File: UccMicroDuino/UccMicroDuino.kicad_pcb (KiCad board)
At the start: 2 copper layers, 8 parts, among them J1 Conn_01x10_Socket, J2 USB_A, U1 ATtiny85-20S

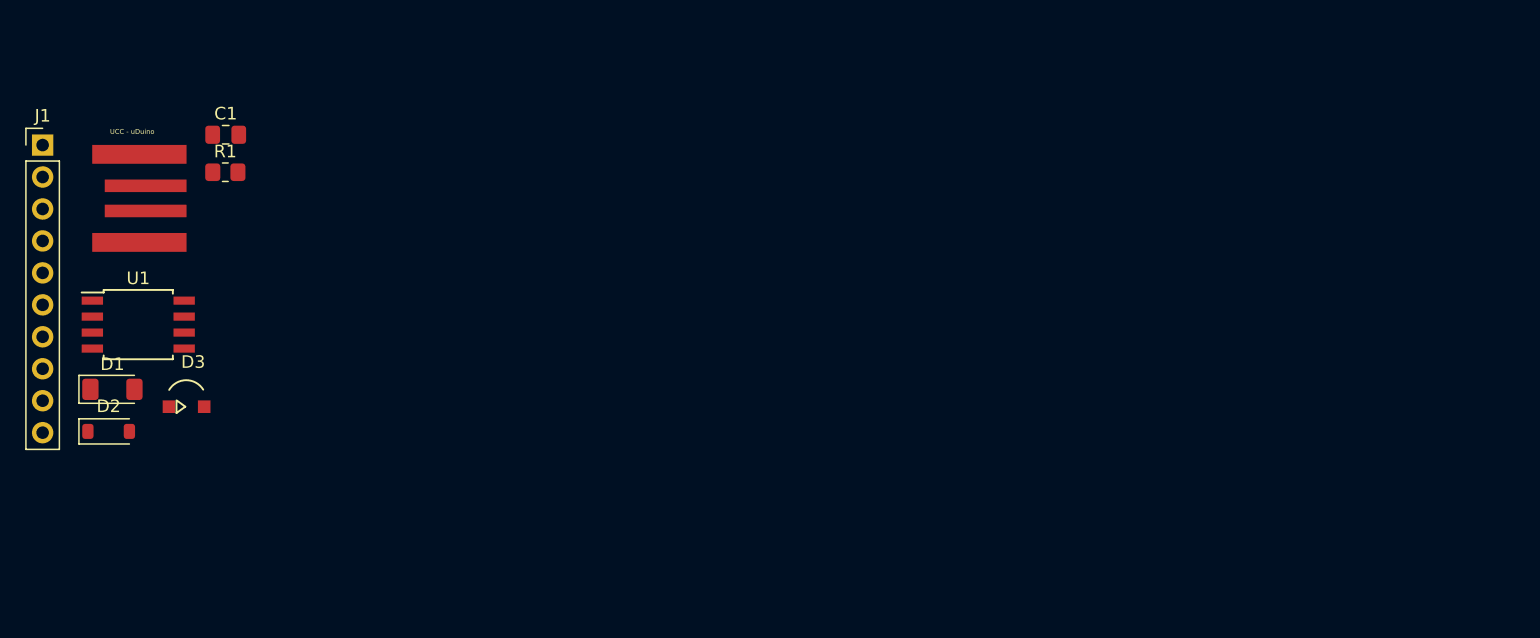
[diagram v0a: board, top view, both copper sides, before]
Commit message: Add files via upload
Subimos el archivo kicad.
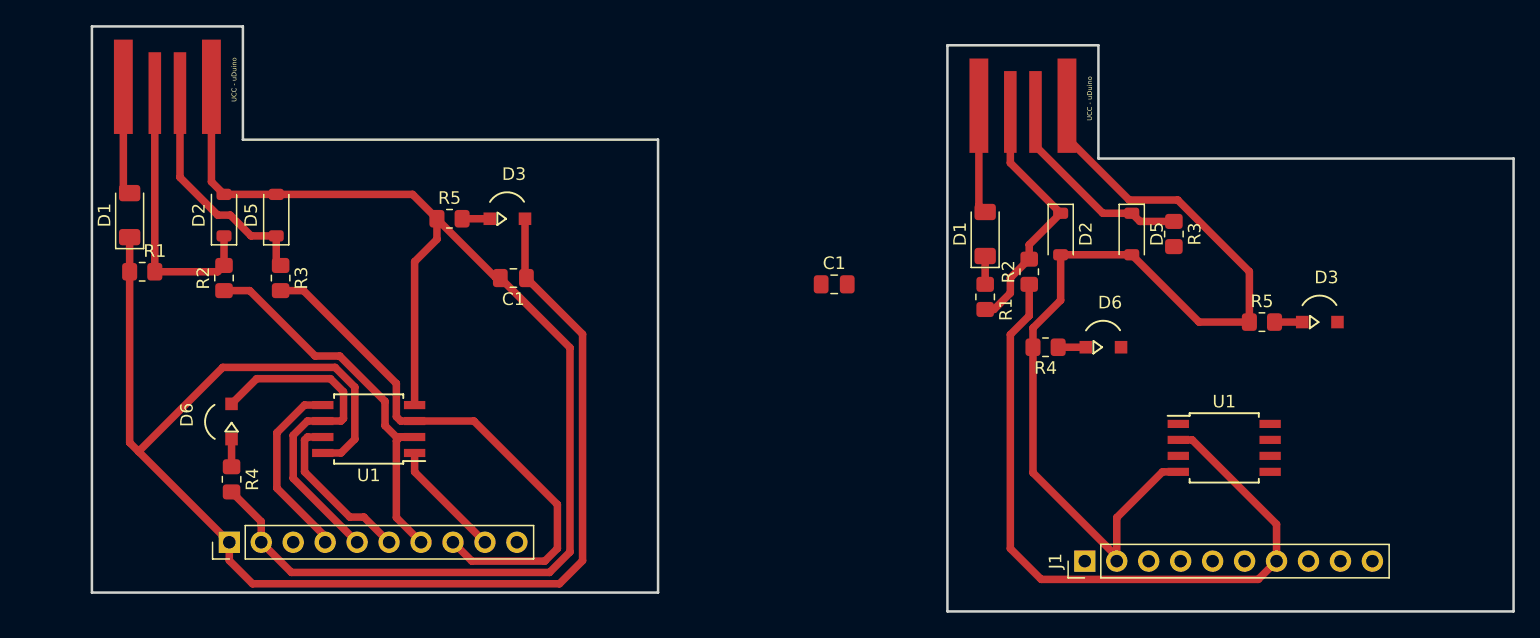
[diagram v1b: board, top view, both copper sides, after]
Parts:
- added C1: C, Capacitor_SMD:C_0805_2012Metric_Pad1.18x1.45mm_HandSolder, F.Cu at (161.5, 78.5)
- added D1: PMLL4148L, Diode_SMD:D_MiniMELF, F.Cu at (131.0, 73.5)
- added D2: 3.6V 1/2mW, Diode_SMD:D_SOD-123, F.Cu at (138.5, 73.5)
- added D3: LED, ledSmd:ledSMD, F.Cu at (161.4, 73.8)
- added D5: 3.6V 1/2mW, Diode_SMD:D_SOD-123, F.Cu at (210.7, 75.0)
- added D5: 3.6V 1/2mW, Diode_SMD:D_SOD-123, F.Cu at (142.7, 73.5)
- added D6: Led Greeen, ledSmd:ledSMD, F.Cu at (139.1, 89.5)
- added D6: Led Greeen, ledSmd:ledSMD, F.Cu at (208.8, 84.0)
- added J1: Header, Connector_PinHeader_2.54mm:PinHeader_1x10_P2.54mm_Vertical, F.Cu at (138.9, 99.5)
- added J2: USB_A, embeddedPcbUsb:USB_A_UCC, F.Cu at (134.0, 63.5)
- added R1: 1.5KΩ 5% 1/8W, Resistor_SMD:R_0805_2012Metric_Pad1.20x1.40mm_HandSolder, F.Cu at (132.0, 78.0)
- added R2: 68 Ω 5% 1/8W, Resistor_SMD:R_0805_2012Metric_Pad1.20x1.40mm_HandSolder, F.Cu at (202.5, 78.0)
- added R2: 68 Ω 5% 1/8W, Resistor_SMD:R_0805_2012Metric_Pad1.20x1.40mm_HandSolder, F.Cu at (138.5, 78.5)
- added R3: 68 Ω 5% 1/8W, Resistor_SMD:R_0805_2012Metric_Pad1.20x1.40mm_HandSolder, F.Cu at (143.0, 78.5)
- added R3: 68 Ω 5% 1/8W, Resistor_SMD:R_0805_2012Metric_Pad1.20x1.40mm_HandSolder, F.Cu at (214.0, 75.0)
- added R4: 330Ω 5%1/8W, Resistor_SMD:R_0805_2012Metric_Pad1.20x1.40mm_HandSolder, F.Cu at (203.8, 84.0)
- added R4: 330Ω 5%1/8W, Resistor_SMD:R_0805_2012Metric_Pad1.20x1.40mm_HandSolder, F.Cu at (139.1, 94.5)
- added R5: 330Ω 5%1/8W, Resistor_SMD:R_0805_2012Metric_Pad1.20x1.40mm_HandSolder, F.Cu at (221.0, 82.0)
- added R5: 330Ω 5%1/8W, Resistor_SMD:R_0805_2012Metric_Pad1.20x1.40mm_HandSolder, F.Cu at (156.4, 73.8)
- added U1: ATtiny85-20S, Package_SO:SOIC-8W_5.3x5.3mm_P1.27mm, F.Cu at (150.0, 90.5)
- D1: value D_Filled -> PMLL4148L
- D2: value D_Zener -> 3.6V 1/2mW
- J1: value Conn_01x10_Socket -> Header
- R1: value R -> 1.5KΩ 5% 1/8W
- moved D3 90.3 mm to (226.0, 82.0)
- moved J1 89.2 mm to (206.9, 101.0), turned to 90 degrees
- moved U1 86.9 mm to (218.0, 92.0)
- moved D2 77.3 mm to (205.0, 75.0), turned to -90 degrees
- moved D1 70.5 mm to (199.0, 75.0), turned to 90 degrees
- moved J2 70.4 mm to (202.0, 65.0), turned to -90 degrees
- moved R1 61.2 mm to (199.0, 80.0), turned to -90 degrees
- moved C1 49.8 mm to (187.0, 79.0)
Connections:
- C1 pad 1: unconnected-(C1-Pad1) -> +5V
- C1 pad 2: unconnected-(C1-Pad2) -> GND
- D1 pad 2: unconnected-(D1-A-Pad2) -> Net-(D1-A)
- D2 pad 1: unconnected-(D2-K-Pad1) -> Net-(D2-K)
- D2 pad 2: unconnected-(D2-A-Pad2) -> GND
- D3 pad 1: unconnected-(D3-K-Pad1) -> Net-(D3-K)
- D3 pad 2: unconnected-(D3-A-Pad2) -> +5V
- J1 pad 1: unconnected-(J1-Pin_1-Pad1) -> +5V
- J1 pad 2: unconnected-(J1-Pin_2-Pad2) -> GND
- J1 pad 4: unconnected-(J1-Pin_4-Pad4) -> Net-(J1-Pin_4)
- J1 pad 5: unconnected-(J1-Pin_5-Pad5) -> Net-(D6-A)
- J1 pad 6: unconnected-(J1-Pin_6-Pad6) -> Net-(J1-Pin_6)
- J1 pad 7: unconnected-(J1-Pin_7-Pad7) -> Net-(J1-Pin_7)
- J1 pad 8: unconnected-(J1-Pin_8-Pad8) -> Net-(J1-Pin_8)
- J1 pad 9: unconnected-(J1-Pin_9-Pad9) -> Net-(J1-Pin_9)
- J2 pad 1: unconnected-(J2-VBUS-Pad1) -> Net-(D1-A)
- J2 pad 2: unconnected-(J2-D--Pad2) -> Net-(D2-K)
- J2 pad 3: unconnected-(J2-D+-Pad3) -> Net-(D5-K)
- J2 pad 4: unconnected-(J2-GND-Pad4) -> GND
- R1 pad 2: unconnected-(R1-Pad2) -> Net-(D2-K)
- U1 pad 1: unconnected-(U1-~{RESET}/PB5-Pad1) -> Net-(J1-Pin_9)
- U1 pad 2: unconnected-(U1-XTAL1/PB3-Pad2) -> Net-(J1-Pin_7)
- U1 pad 3: unconnected-(U1-XTAL2/PB4-Pad3) -> Net-(J1-Pin_8)
- U1 pad 4: unconnected-(U1-GND-Pad4) -> GND
- U1 pad 5: unconnected-(U1-AREF/PB0-Pad5) -> Net-(J1-Pin_4)
- U1 pad 6: unconnected-(U1-PB1-Pad6) -> Net-(D6-A)
- U1 pad 7: unconnected-(U1-PB2-Pad7) -> Net-(J1-Pin_6)
- U1 pad 8: unconnected-(U1-VCC-Pad8) -> +5V
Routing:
- net GND: track 0.00 -> 185.0 mm
- net +5V: track 0.00 -> 117.7 mm
- net Net-(J1-Pin_7): track 0.00 -> 90.9 mm
- net Net-(J1-Pin_8): track 0.00 -> 43.4 mm
- net Net-(D2-K): track 0.00 -> 42.5 mm
- net Net-(D5-K): track 0.00 -> 37.7 mm
- net Net-(D6-A): track 0.00 -> 27.4 mm
- net Net-(D1-A): track 0.00 -> 17.3 mm
- net Net-(J1-Pin_4): track 0.00 -> 14.9 mm
- net Net-(J1-Pin_6): track 0.00 -> 13.1 mm
- net Net-(J1-Pin_9): track 0.00 -> 9.41 mm
- net Net-(D6-K): track 0.00 -> 4.40 mm
- net Net-(D3-K): track 0.00 -> 4.40 mm
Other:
- board outline added: 113 x 46.5 mm
